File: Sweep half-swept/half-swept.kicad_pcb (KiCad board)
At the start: 2 copper layers, 109 x 86.9 mm, 25 parts, among them J2 AudioJack4dpb, SW1 SW_Push, SW10 SW_Push, SW11 SW_Push, SW12 SW_Push, SW13 SW_Push, SW14 SW_Push, SW15 SW_Push, SW16 SW_Push, SW17 SW_Push, SW2 SW_Push, SW3 SW_Push, SW4 SW_Push, SW5 SW_Push, SW6 SW_Push, SW7 SW_Push, SW8 SW_Push, SW9 SW_Push, U1 ProMicro-kbd

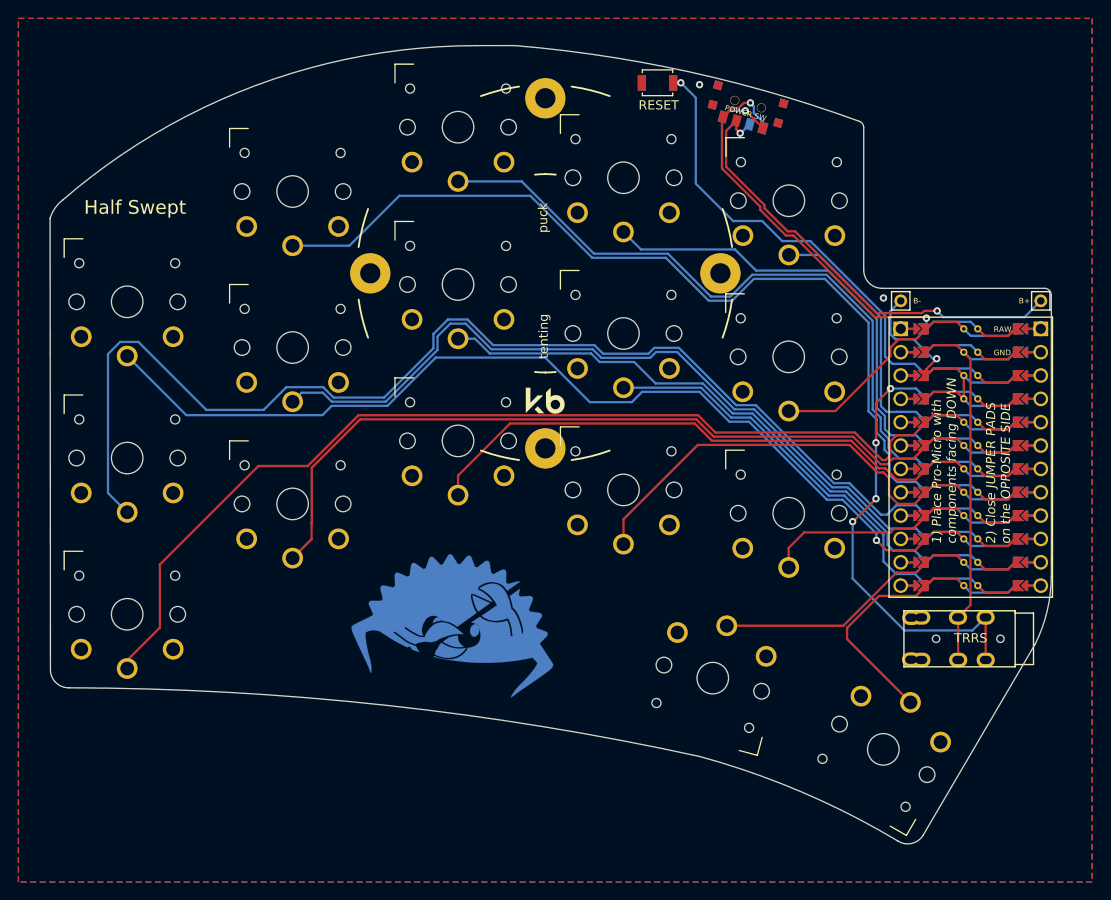
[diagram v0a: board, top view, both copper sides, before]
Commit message: Make PCB follow switch outline instead of arc
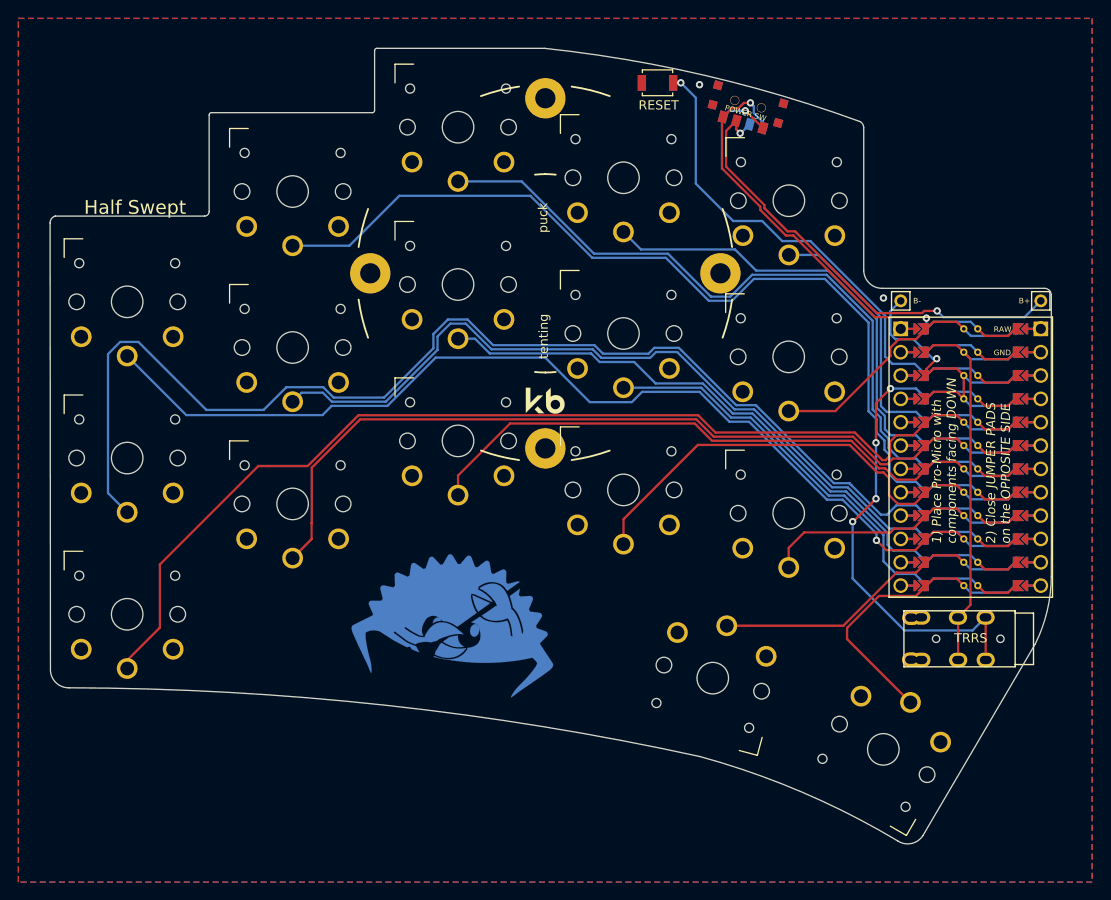
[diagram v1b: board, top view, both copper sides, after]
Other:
- board size 109 x 86.9 mm -> 109 x 86.6 mm

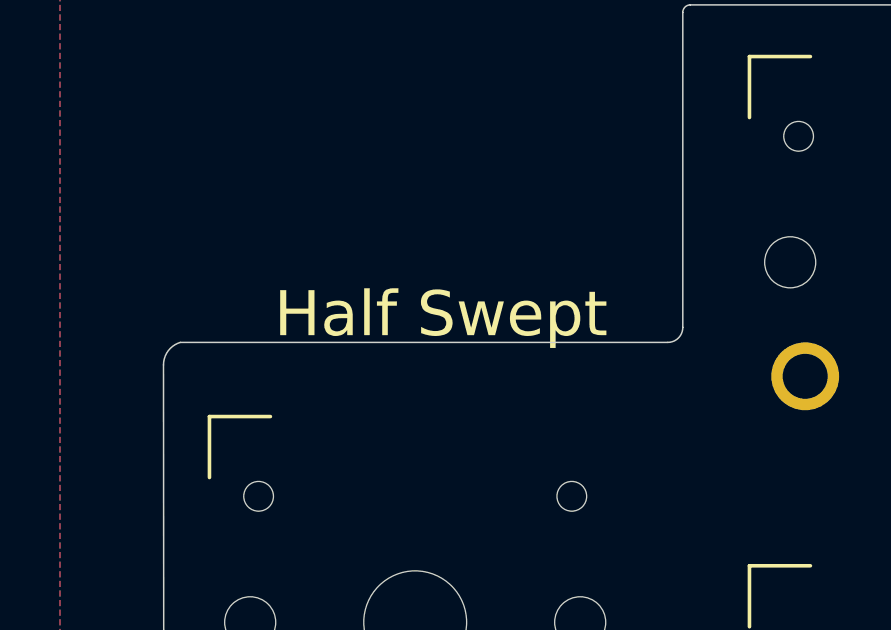
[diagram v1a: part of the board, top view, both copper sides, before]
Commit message: Remove Half Swept silkscreen
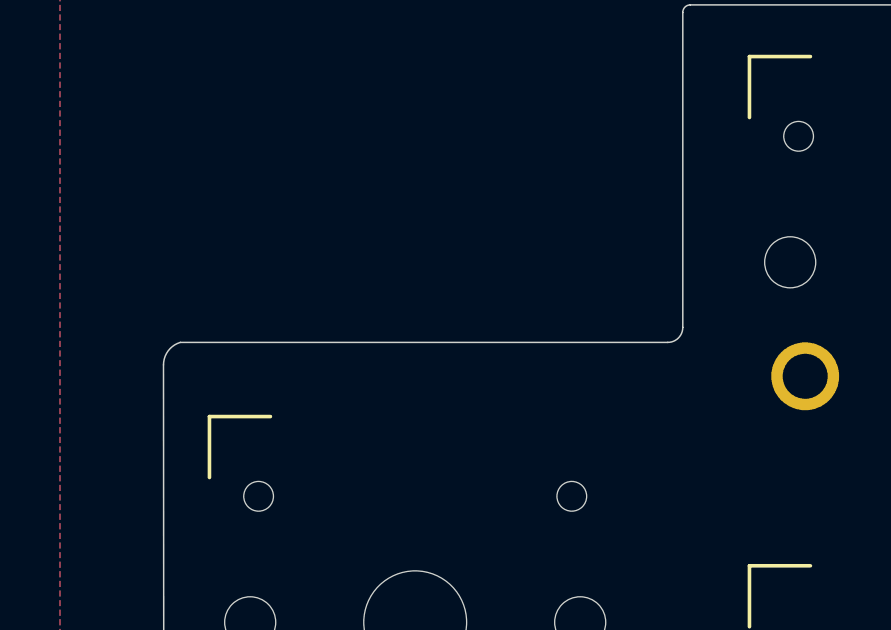
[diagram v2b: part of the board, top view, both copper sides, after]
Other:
- board text removed: "Half Swept"
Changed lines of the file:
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@@
     (effects (font (size 1 1) (thickness 0.15) italic) (justify left))
-  )
-  (gr_text "Half Swept" (at 27.94 35.814) (layer "F.SilkS")
-    (effects (font (size 1.5 1.5) (thickness 0.3)))
   )
   (gr_text "GND" (at 121.3612 51.6128) (layer "F.SilkS")
